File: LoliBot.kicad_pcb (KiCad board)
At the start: 2 copper layers, 146 x 100 mm, 41 parts, among them J1 LOLINBATT, J10 LEFT-MOTOR, J11 REFLECT_, J12 MECH, J13 MECH, J14 MECH, J15 MECH, J16 MECH, J17 MECH, J18 MECH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

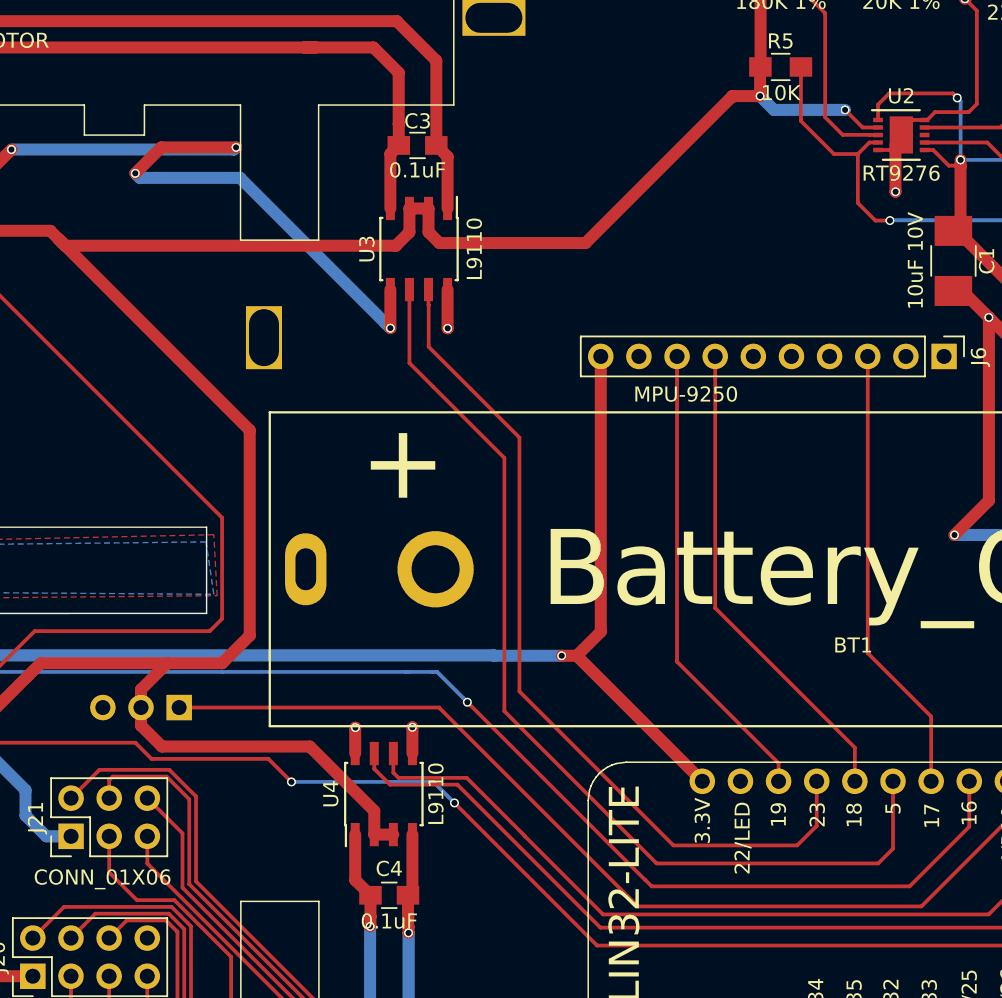
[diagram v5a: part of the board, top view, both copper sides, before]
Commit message: Moved Servo position
to remove interference with expansion ports.
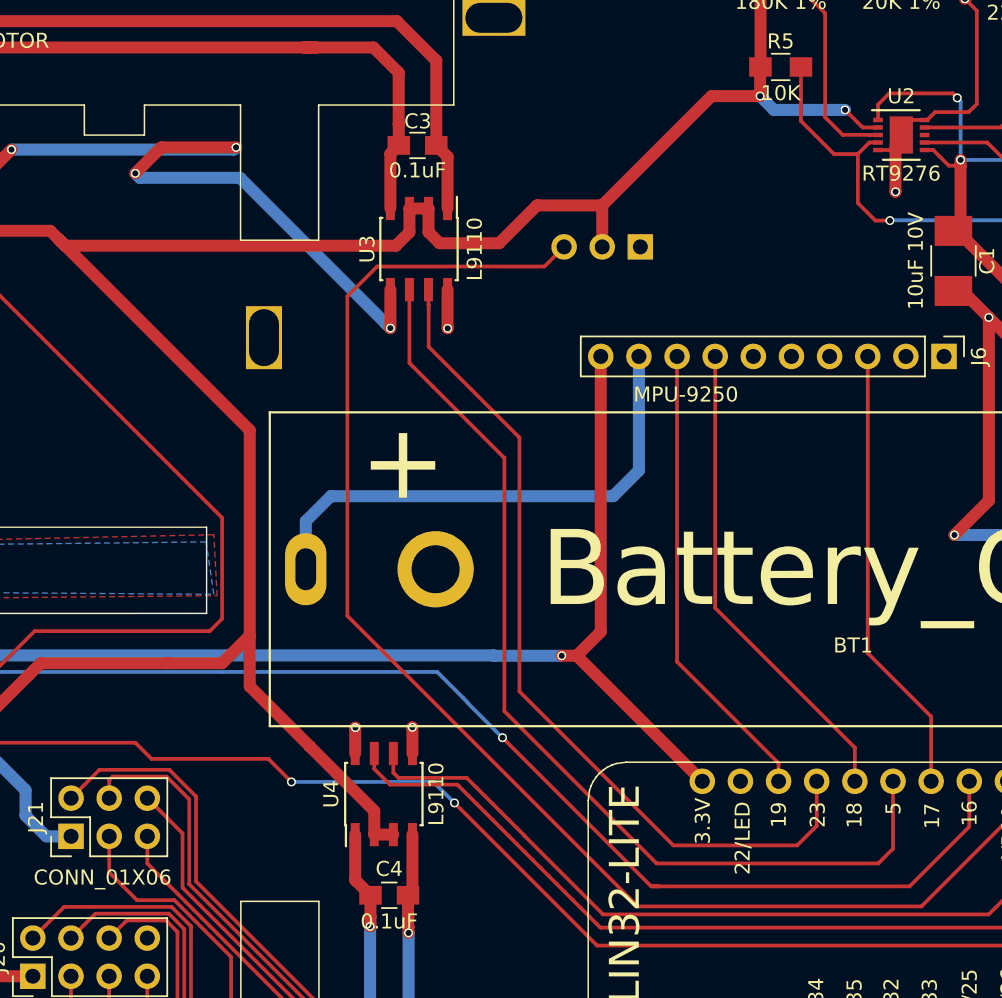
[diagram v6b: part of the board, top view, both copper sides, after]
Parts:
- J3: footprint Pin_Headers:Pin_Header_Straight_1x03_Pitch2.54mm -> Pin_Headers:Pin_Header_Angled_1x03_Pitch2.54mm
- moved J3 43.4 mm to (130.8, 67.7)
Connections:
- J3 pad 1: /IO4 -> GND
- J3 pad 3: GND -> /IO4
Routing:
- net GND: track 157.1 -> 191.5 mm
- net /IO4: track 65.6 -> 94.0 mm
- net +5V: track 320.3 -> 315.4 mm

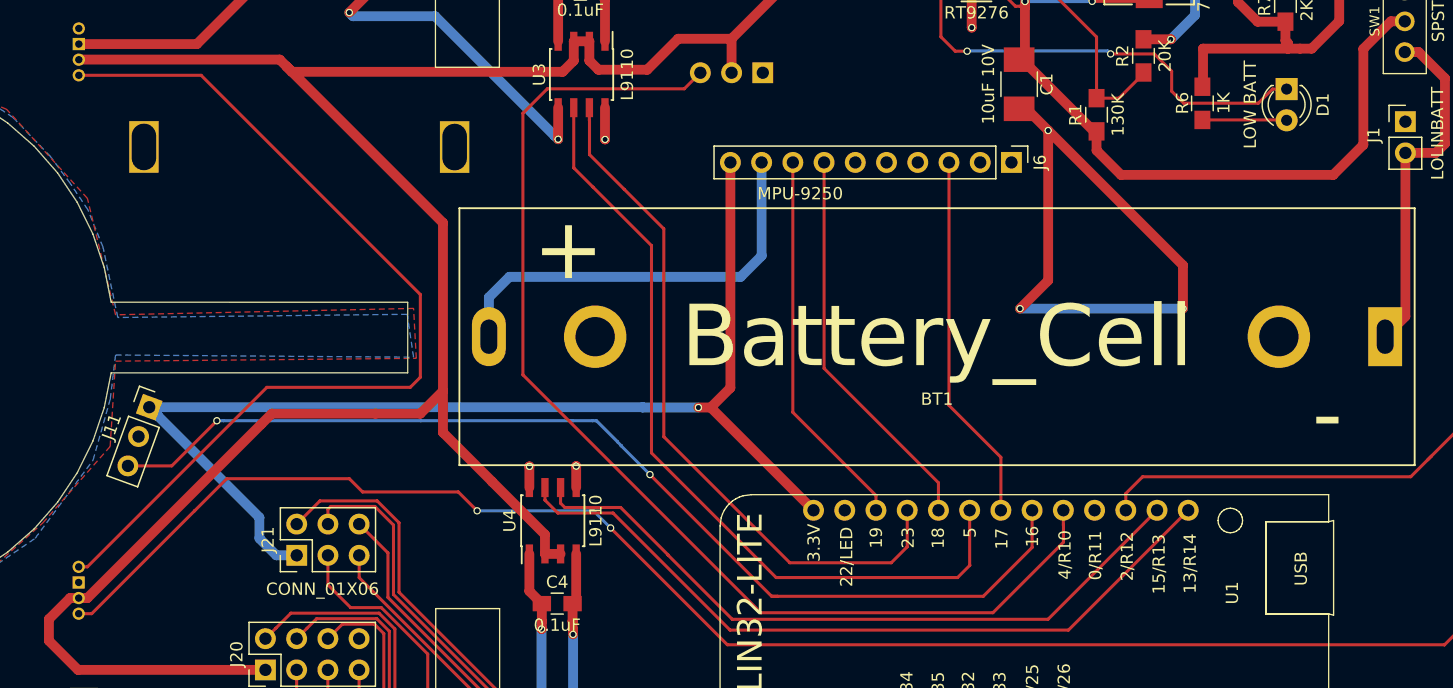
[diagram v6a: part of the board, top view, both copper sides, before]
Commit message: battery symbols reversed.
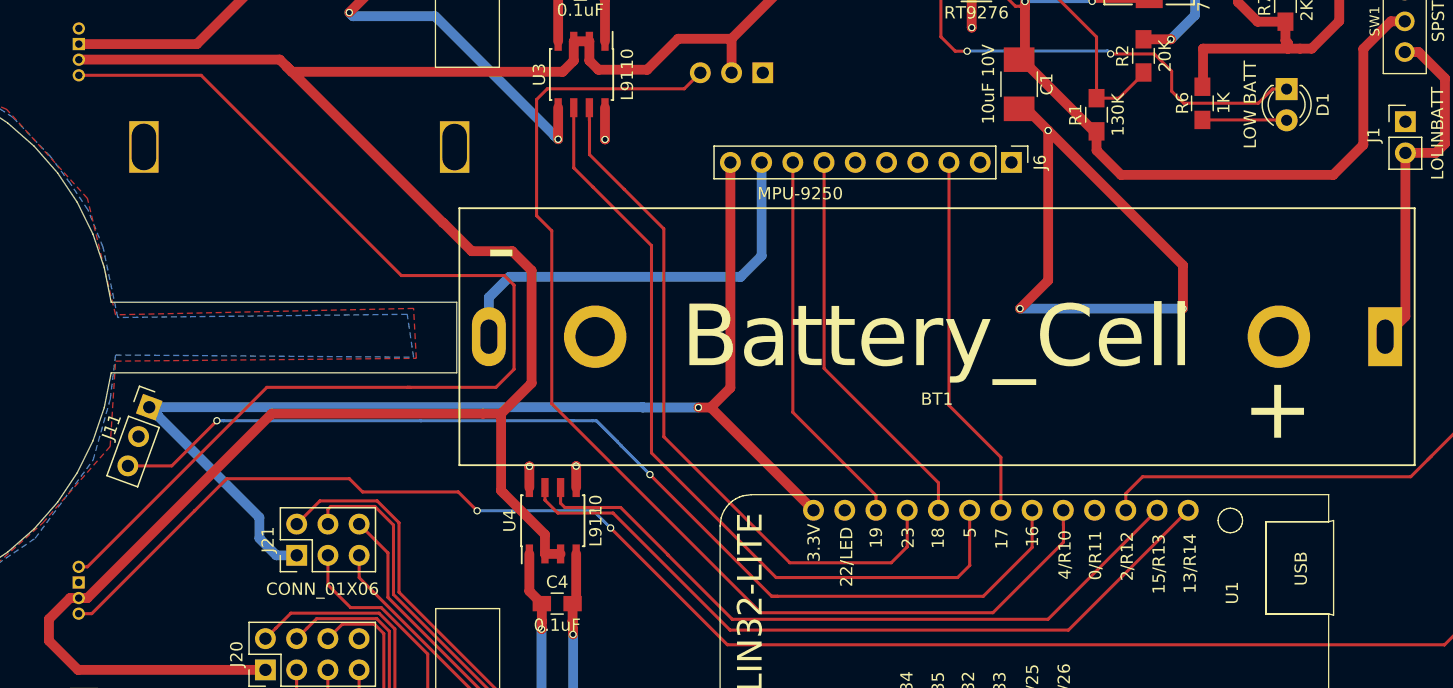
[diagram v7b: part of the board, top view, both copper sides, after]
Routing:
- net Net-(J7-Pad4): track 76.1 -> 91.6 mm
- net +5V: track 315.4 -> 323.3 mm
- net /IO4: track 94.0 -> 93.1 mm
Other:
- outline, holes or cut-outs redrawn

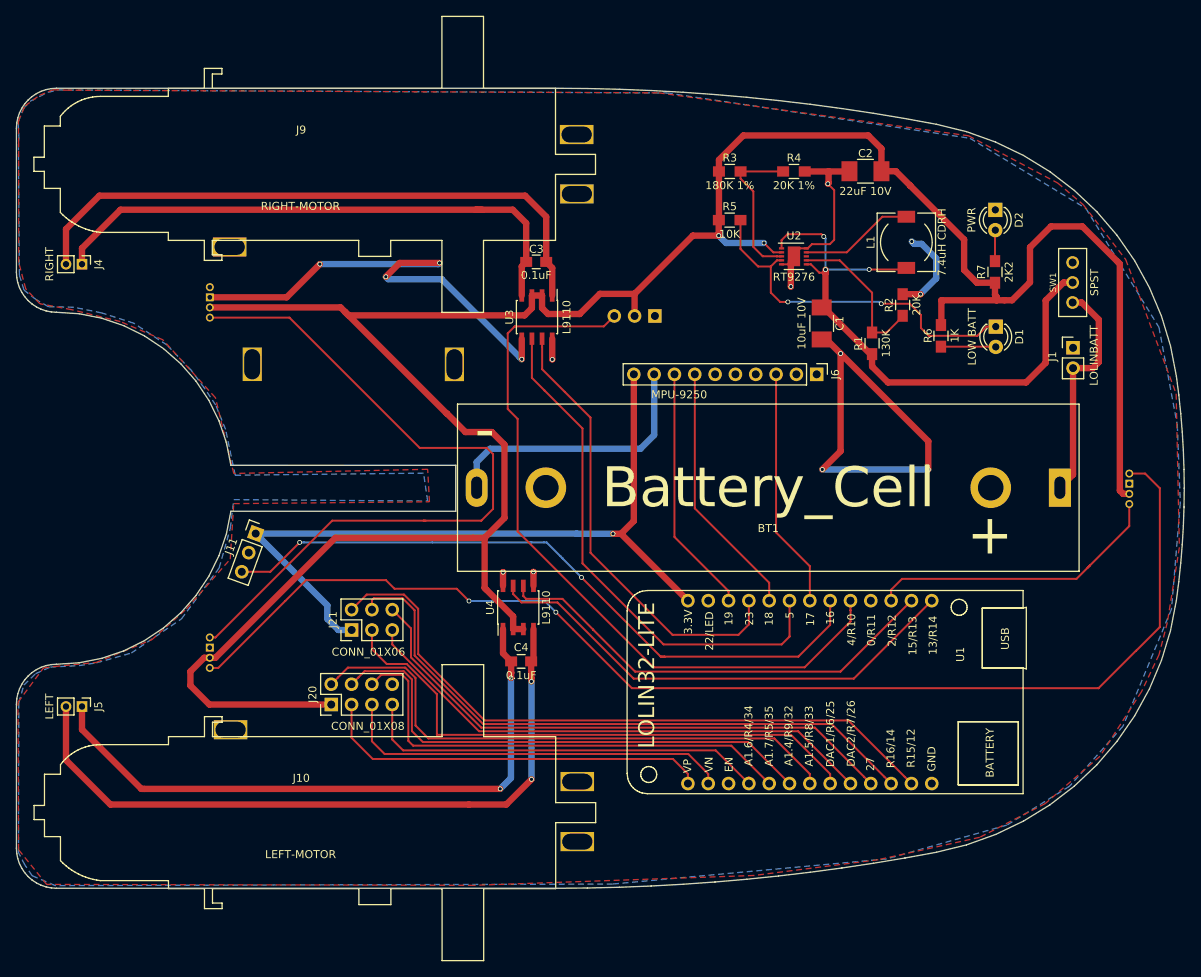
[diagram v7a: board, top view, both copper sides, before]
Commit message: Removed voltage boost.
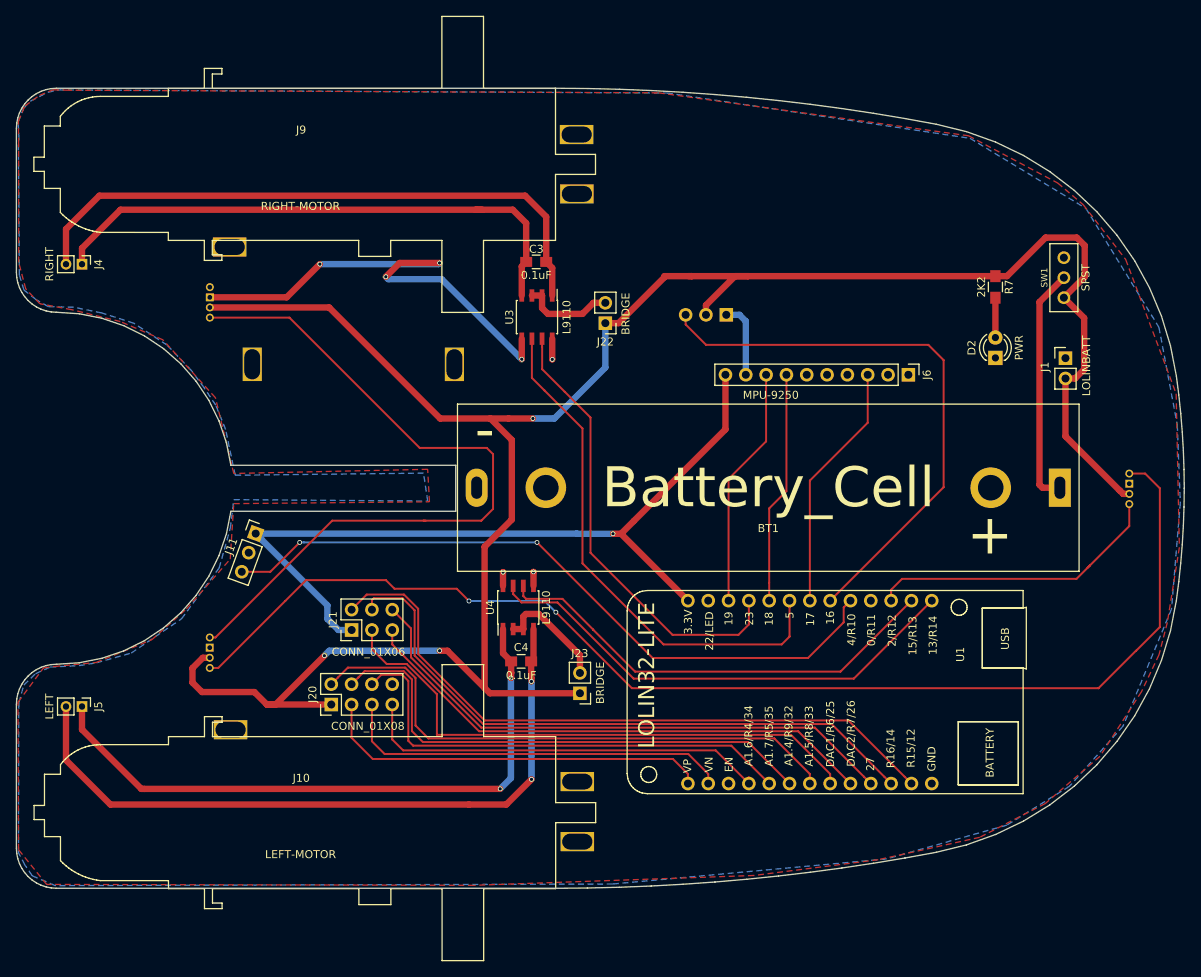
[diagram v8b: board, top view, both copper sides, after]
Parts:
- removed C1: 10uF 10V, Capacitors_SMD:C_1210_HandSoldering
- removed C2: 22uF 10V, Capacitors_SMD:C_1210_HandSoldering
- removed D1: LOW BATT, LEDs:LED_D3.0mm
- removed L1: 7.4uH CDRH, Choke_SMD:Choke_SMD_7.3x7.3_H3.5
- removed R1: 130K, Resistors_SMD:R_0805_HandSoldering
- removed R2: 20K, Resistors_SMD:R_0805_HandSoldering
- removed R3: 180K 1%, Resistors_SMD:R_0805_HandSoldering
- removed R4: 20K 1%, Resistors_SMD:R_0805_HandSoldering
- removed R5: 10K, Resistors_SMD:R_0805_HandSoldering
- removed R6: 1K, Resistors_SMD:R_0805_HandSoldering
- removed U2: RT9276, Housings_DFN_QFN:DFN-10-1EP_3x3mm_Pitch0.5mm
- added J22: BRIDGE, Pin_Headers:Pin_Header_Straight_1x02_Pitch2.54mm, F.Cu at (124.6, 68.6)
- added J23: BRIDGE, Pin_Headers:Pin_Header_Straight_1x02_Pitch2.54mm, F.Cu at (121.4, 114.9)
- moved D2 18.5 mm to (173.4, 73.0), turned to 90 degrees
- moved J6 11.5 mm to (162.5, 75.1)
- moved J3 8.92 mm to (139.7, 67.6)
- moved R7 1.88 mm to (173.4, 64.1), turned to 270 degrees
- moved J1 1.60 mm to (182.1, 73.0)
- moved SW1 1.25 mm to (181.9, 62.9)
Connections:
- J1 pad 2: Net-(BT1-Pad1) -> /BATT_V
- J11 pad 3: /IO16 -> /IO4
- J2 pad 2: +5V -> /BATT_V
- J20 pad 1: +5V -> /BATT_V
- J3 pad 2: +5V -> /BATT_V
- J3 pad 3: /IO4 -> /IO16
- J7 pad 2: +5V -> /BATT_V
- J8 pad 2: +5V -> /BATT_V
- R7 pad 1: +5V -> /BATT_V
- SW1 pad 1: Net-(BT1-Pad1) -> /BATT_V
- SW1 pad 2: Net-(C1-Pad1) -> Net-(BT1-Pad1)
- U3 pad 2: +5V -> Net-(J22-Pad2)
- U3 pad 3: +5V -> Net-(J22-Pad2)
- U4 pad 2: +5V -> Net-(J23-Pad2)
- U4 pad 3: +5V -> Net-(J23-Pad2)
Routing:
- net +5V: track 323.3 -> 0.00 mm, vias 2 -> 0
- net /BATT_V: track 0.00 -> 278.5 mm, vias 0 -> 3
- net GND: track 191.5 -> 77.3 mm, vias 14 -> 7
- net Net-(C1-Pad1): track 75.1 -> 0.00 mm, vias 3 -> 0
- net /LBO: track 45.1 -> 0.00 mm, vias 2 -> 0
- net Net-(R1-Pad2): track 19.6 -> 0.00 mm
- net Net-(R3-Pad2): track 19.4 -> 0.00 mm
- net /IO16: track 86.4 -> 71.2 mm, vias 2 -> 0
- net Net-(J23-Pad2): track 0.00 -> 14.4 mm
- net Net-(L1-Pad2): track 14.3 -> 0.00 mm
- net Net-(J22-Pad2): track 0.00 -> 11.6 mm
- net Net-(D1-Pad2): track 6.86 -> 0.00 mm
- net /IO4: track 93.1 -> 87.7 mm, vias 0 -> 2
- net +3V3: track 96.1 -> 100.8 mm
- net /IO18: track 31.9 -> 28.9 mm
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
